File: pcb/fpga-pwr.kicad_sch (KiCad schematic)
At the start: 8 parts, among them M1V? TestPoint

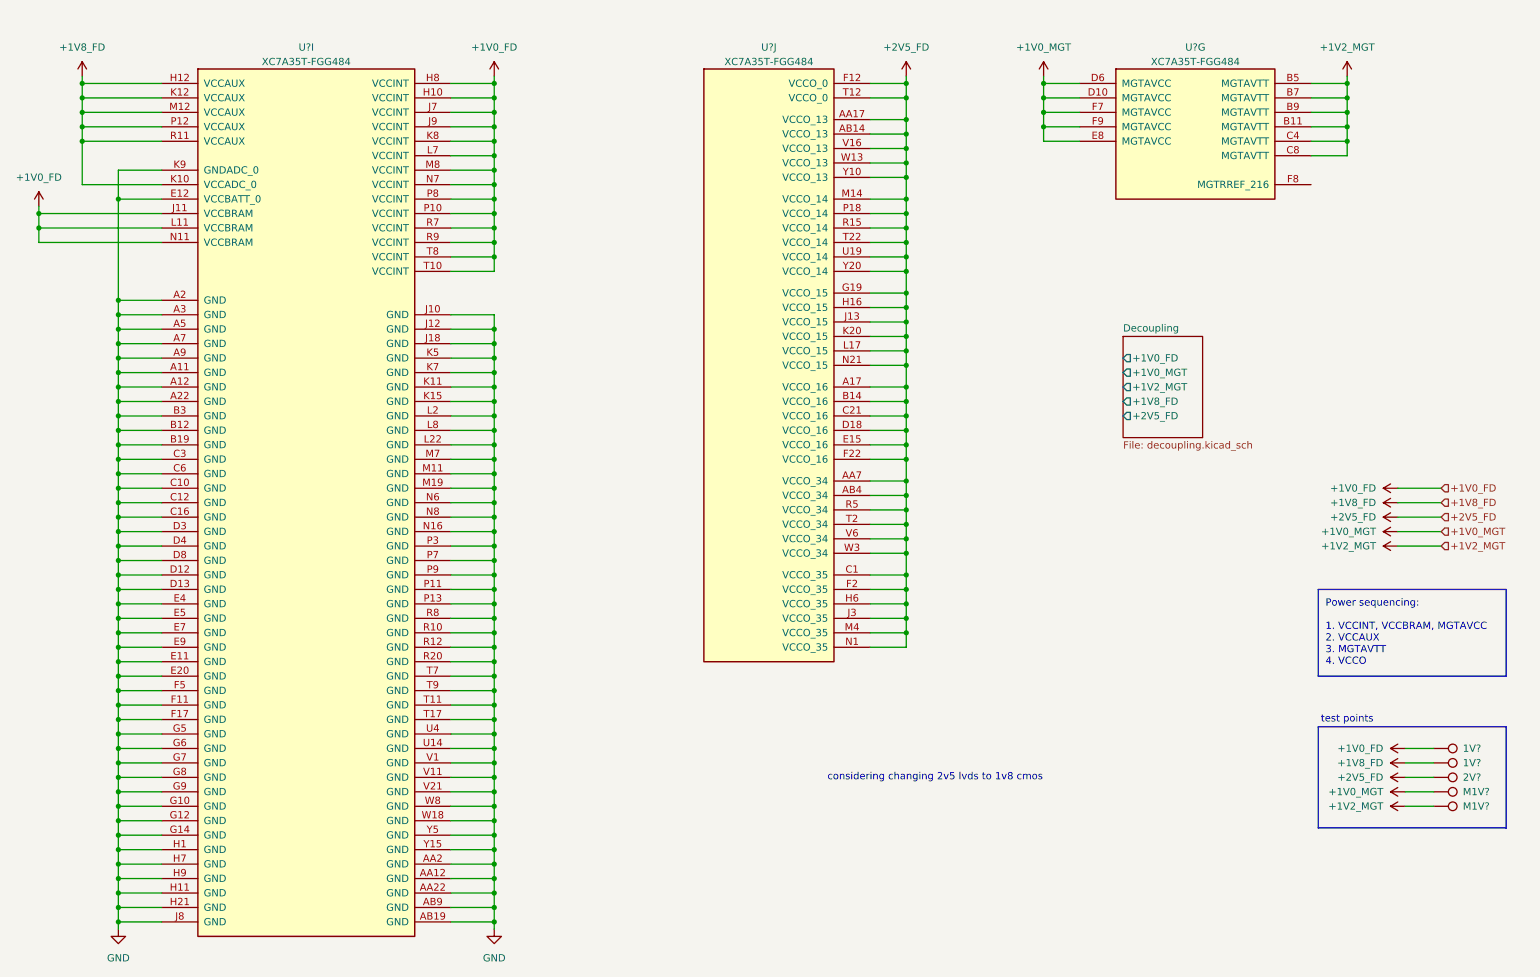
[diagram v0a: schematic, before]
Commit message: completed bus aliasing definitions
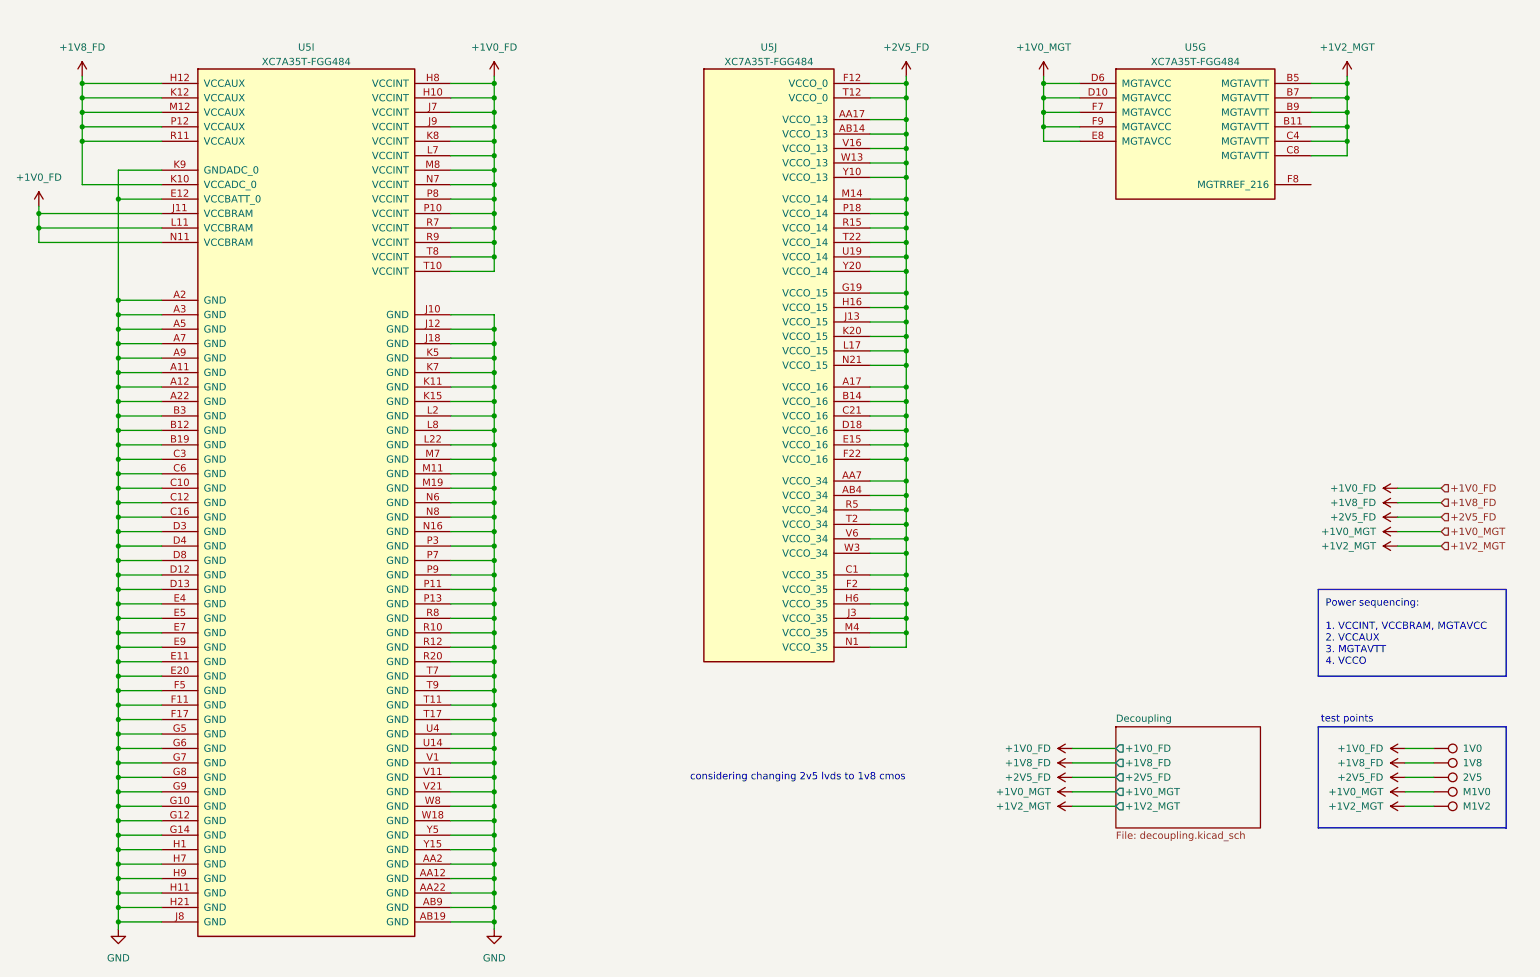
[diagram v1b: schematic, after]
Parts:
- gave numbers to parts that had none: 6

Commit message: updated sims, power hierarchy
added power flags to voltage buses, removed standard kicad "+3.3V" power flags and using standard kicad "power flag" in order to use hierarchical labels to visually show power paths
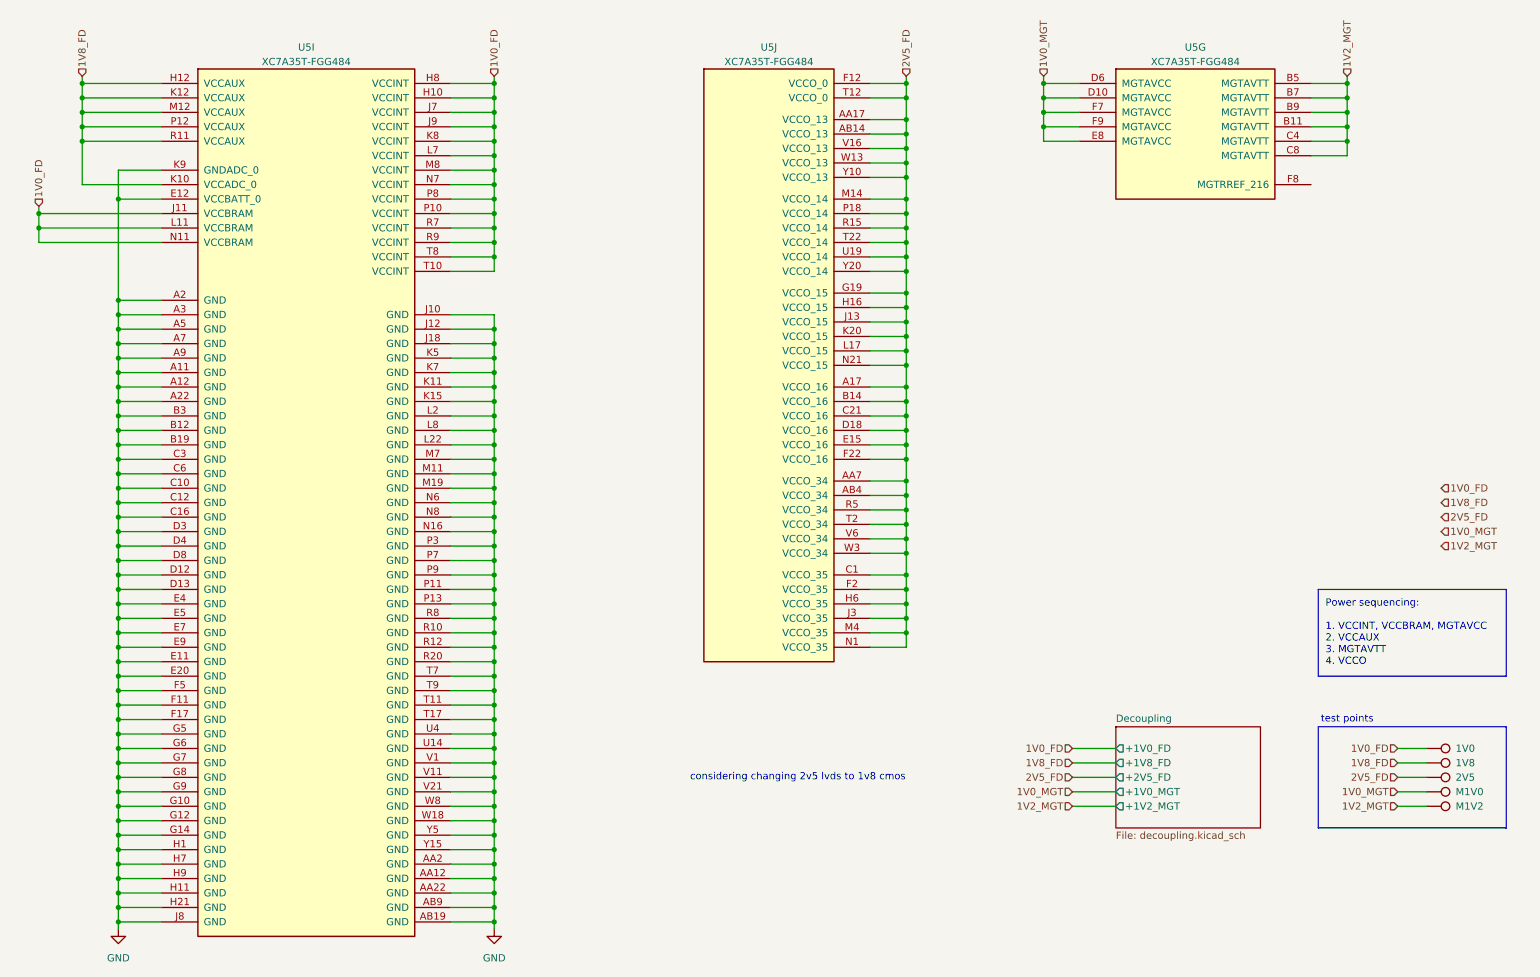
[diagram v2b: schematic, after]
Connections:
- net +1V0_FD renamed 1V0_FD
- net +1V0_MGT renamed 1V0_MGT
- net +1V2_MGT renamed 1V2_MGT
- net +1V8_FD renamed 1V8_FD
- net +2V5_FD renamed 2V5_FD
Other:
- moved on the sheet: 1V0, 1V8, 2V5, M1V0, M1V2

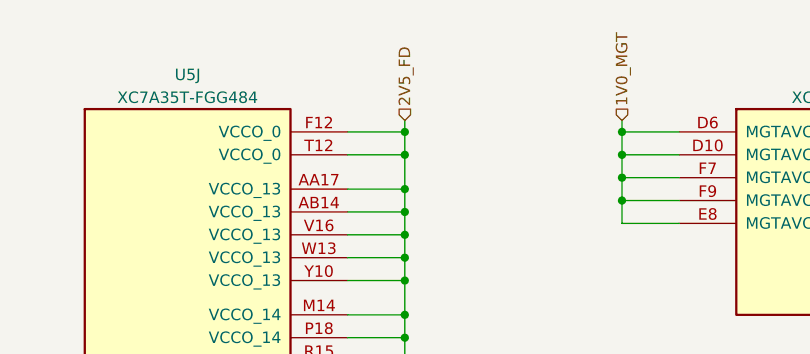
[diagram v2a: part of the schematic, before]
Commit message: restructured power hierarchy
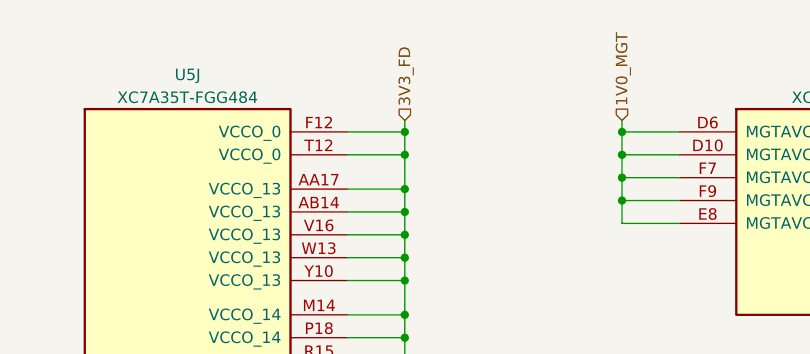
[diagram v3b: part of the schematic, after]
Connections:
- net 2V5_FD: no longer U5.A17 (VCCO_16), U5.AA17 (VCCO_13), U5.AA7 (VCCO_34), U5.AB14 (VCCO_13), U5.AB4 (VCCO_34), U5.B14 (VCCO_16), U5.C1 (VCCO_35), U5.C21 (VCCO_16), U5.D18 (VCCO_16), U5.E15 (VCCO_16), U5.F12 (VCCO_0), U5.F2 (VCCO_35), U5.F22 (VCCO_16), U5.G19 (VCCO_15), U5.H16 (VCCO_15), U5.H6 (VCCO_35), U5.J13 (VCCO_15), U5.J3 (VCCO_35), U5.K20 (VCCO_15), U5.L17 (VCCO_15), U5.M14 (VCCO_14), U5.M4 (VCCO_35), U5.N1 (VCCO_35), U5.N21 (VCCO_15), U5.P18 (VCCO_14), U5.R15 (VCCO_14), U5.R5 (VCCO_34), U5.T12 (VCCO_0), U5.T2 (VCCO_34), U5.T22 (VCCO_14), U5.U19 (VCCO_14), U5.V16 (VCCO_13), U5.V6 (VCCO_34), U5.W13 (VCCO_13), U5.W3 (VCCO_34), U5.Y10 (VCCO_13), U5.Y20 (VCCO_14)
- new net 3V3_FD: U5.A17 (VCCO_16), U5.AA17 (VCCO_13), U5.AA7 (VCCO_34), U5.AB14 (VCCO_13), U5.AB4 (VCCO_34), U5.B14 (VCCO_16), U5.C1 (VCCO_35), U5.C21 (VCCO_16), U5.D18 (VCCO_16), U5.E15 (VCCO_16), U5.F12 (VCCO_0), U5.F2 (VCCO_35), U5.F22 (VCCO_16), U5.G19 (VCCO_15), U5.H16 (VCCO_15), U5.H6 (VCCO_35), U5.J13 (VCCO_15), U5.J3 (VCCO_35), U5.K20 (VCCO_15), U5.L17 (VCCO_15), U5.M14 (VCCO_14), U5.M4 (VCCO_35), U5.N1 (VCCO_35), U5.N21 (VCCO_15), U5.P18 (VCCO_14), U5.R15 (VCCO_14), U5.R5 (VCCO_34), U5.T12 (VCCO_0), U5.T2 (VCCO_34), U5.T22 (VCCO_14), U5.U19 (VCCO_14), U5.V16 (VCCO_13), U5.V6 (VCCO_34), U5.W13 (VCCO_13), U5.W3 (VCCO_34), U5.Y10 (VCCO_13), U5.Y20 (VCCO_14)
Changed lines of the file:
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@@
 		)
 	)
-	(hierarchical_label "2V5_FD"
+	(hierarchical_label "3V3_FD"
 		(shape input)
 		(at 172.72 27.94 90)

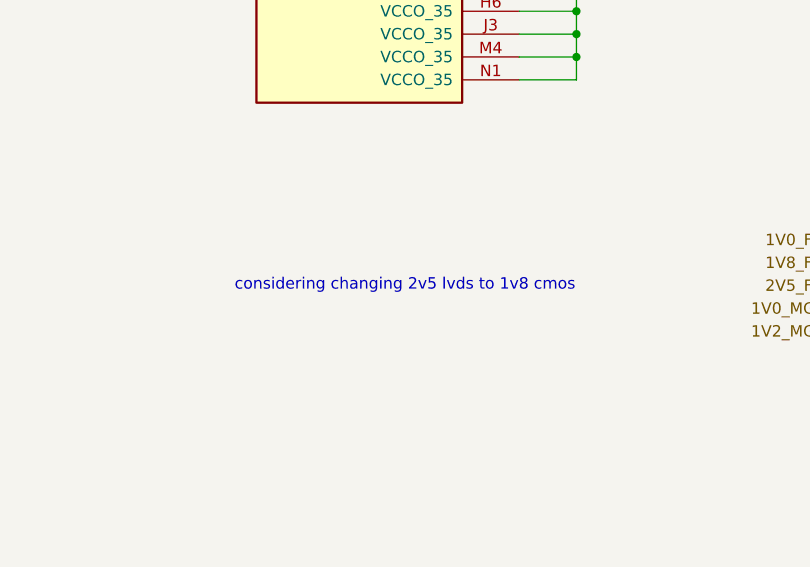
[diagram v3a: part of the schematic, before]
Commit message: power supply comp abstraction
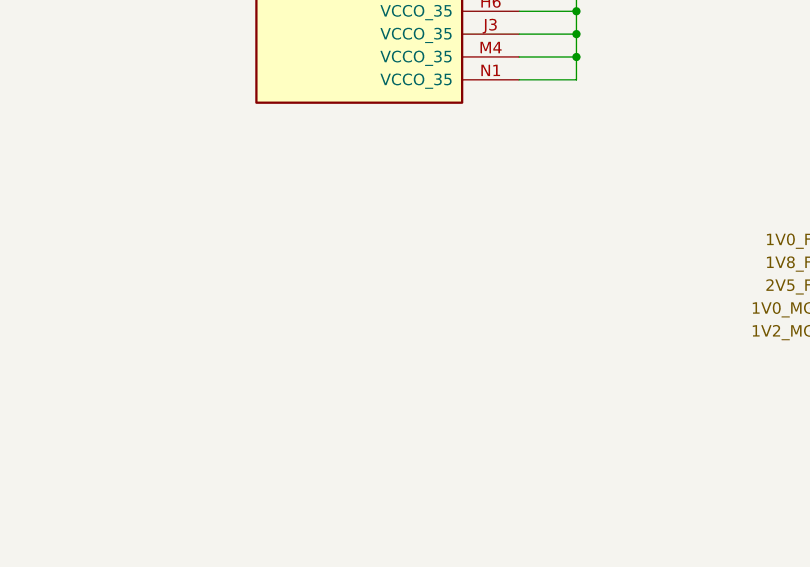
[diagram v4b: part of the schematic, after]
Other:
- note removed: "considering changing 2v5 lvds to 1v8 cmos"
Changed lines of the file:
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@@
-		)
-	)
-	(text "considering changing 2v5 lvds to 1v8 cmos"
-		(exclude_from_sim no)
-		(at 153.67 151.13 0)
-		(effects
-			(font
-				(size 1.27 1.27)
-			)
 		)
 	)

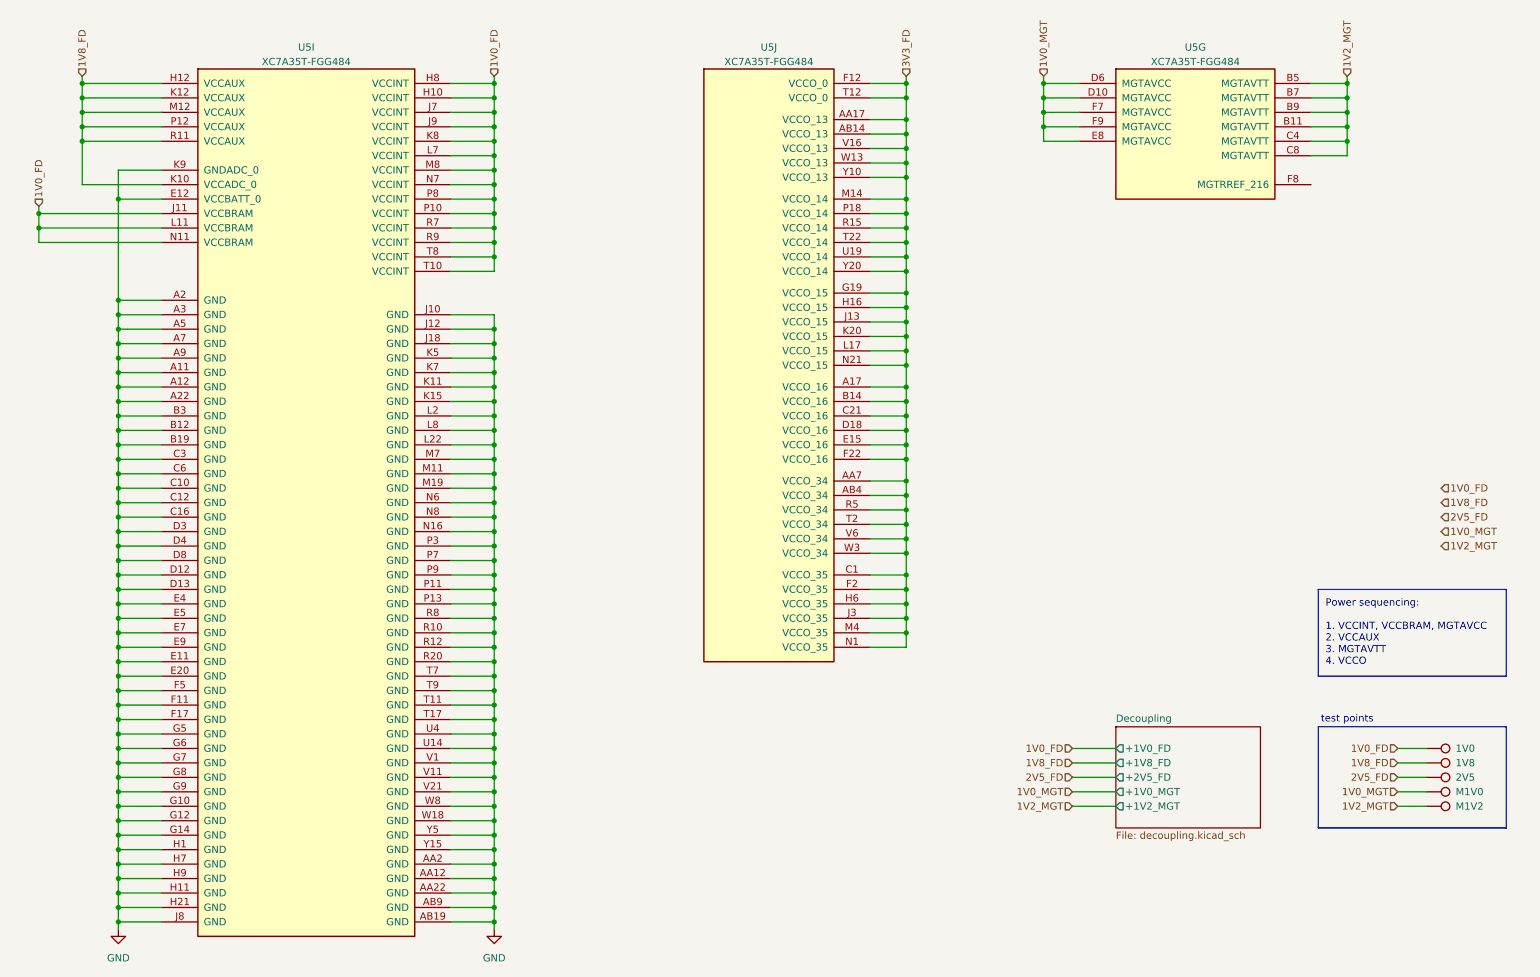
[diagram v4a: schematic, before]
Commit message: current sense hierarchy definition
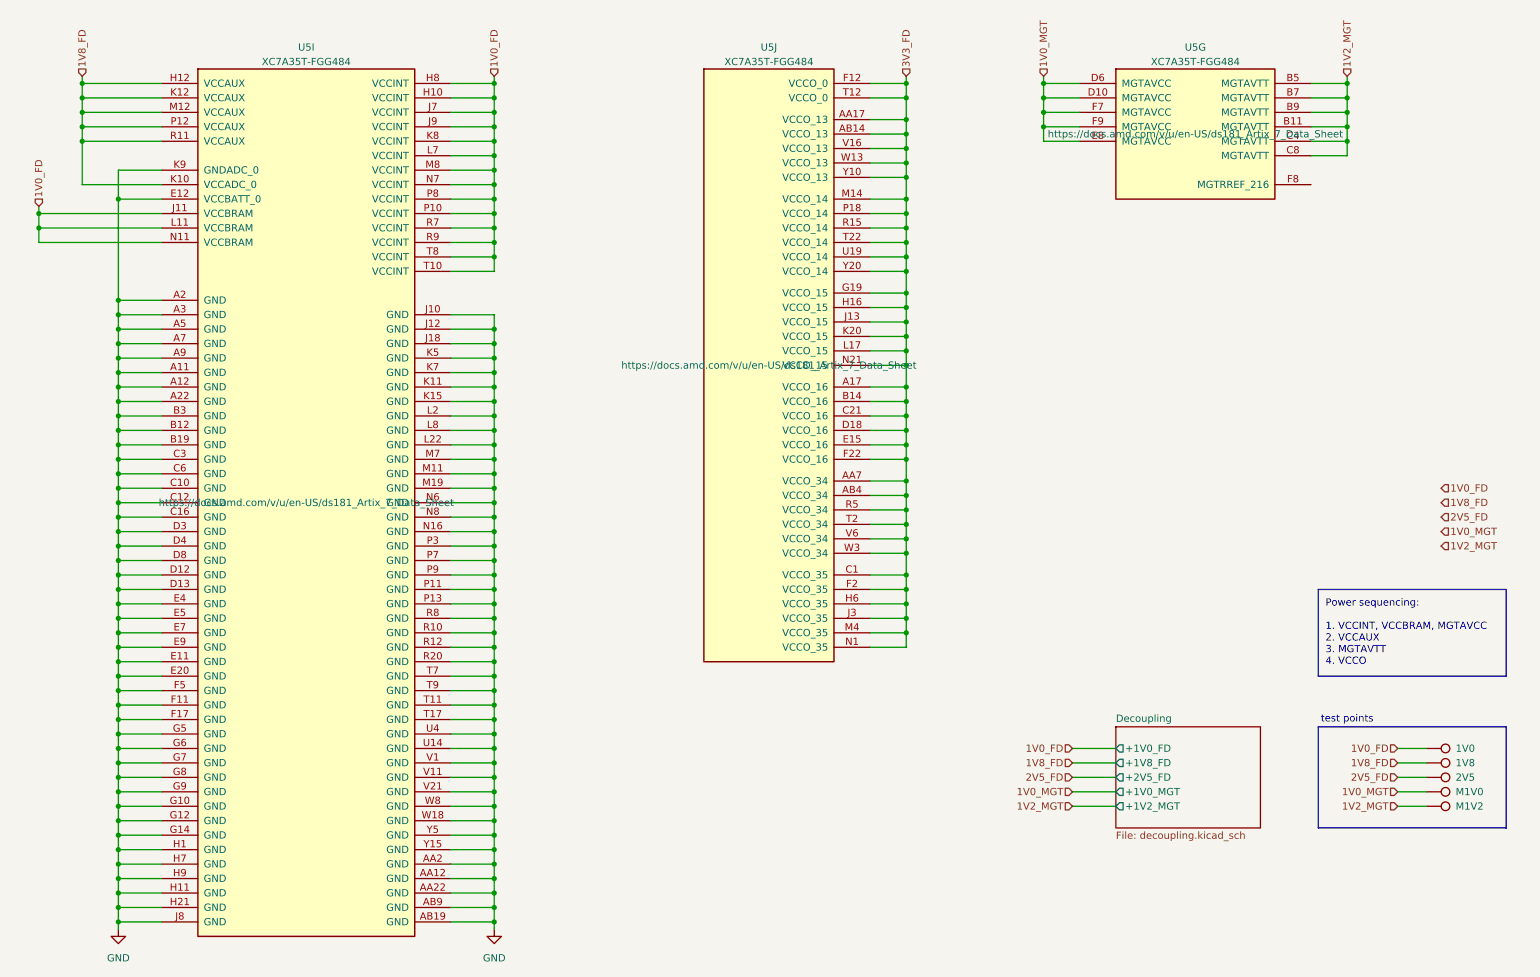
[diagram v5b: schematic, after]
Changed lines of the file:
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@@
 			)
 		)
-		(property "Datasheet" ""
+		(property "Datasheet" "https://docs.amd.com/v/u/en-US/ds181_Artix_7_Data_Sheet"
 			(at 223.52 38.1 0)
 			(effects
@@
 			)
 		)
-		(property "Description" "Artix 7 T 35 XC7A35T-FGG484"
+		(property "Description" "XC7A35T-FGG484"
 			(at 196.85 21.59 0)
+			(effects
+				(font
+					(size 1.27 1.27)
+				)
+				(hide yes)
+			)
+		)
+		(property "Name" ""
+			(at 223.52 38.1 0)
 			(effects
 				(font
@@
 			)
 		)
-		(property "Datasheet" ""
+		(property "Datasheet" "https://docs.amd.com/v/u/en-US/ds181_Artix_7_Data_Sheet"
 			(at 148.59 78.74 0)
 			(effects
@@
 			)
 		)
-		(property "Description" "Artix 7 T 35 XC7A35T-FGG484"
+		(property "Description" "XC7A35T-FGG484"
 			(at 121.92 62.23 0)
+			(effects
+				(font
+					(size 1.27 1.27)
+				)
+				(hide yes)
+			)
+		)
+		(property "Name" ""
+			(at 148.59 78.74 0)
 			(effects
 				(font
@@
 			)
 		)
-		(property "Datasheet" ""
+		(property "Datasheet" "https://docs.amd.com/v/u/en-US/ds181_Artix_7_Data_Sheet"
 			(at 67.31 102.87 0)
 			(effects
@@
 			)
 		)
-		(property "Description" "Artix 7 T 35 XC7A35T-FGG484"
+		(property "Description" "XC7A35T-FGG484"
 			(at 40.64 86.36 0)
 			(effects
 				(font
+					(size 1.27 1.27)
+				)
+				(hide yes)
+			)
+		)
+		(property "Name" ""
+			(at 67.31 102.87 0)
+			(effects
+				(font
